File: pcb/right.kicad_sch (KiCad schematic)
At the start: 63 parts, among them J201 Conn_01x06_MountingPin, SW201 SW_SPDT, SW43 SW_Push, SW44 SW_Push, SW45 SW_Push, SW46 SW_Push, SW47 SW_Push, SW48 SW_Push, SW50 SW_Push, SW51 SW_Push, SW52 SW_Push, SW53 SW_Push, SW54 SW_Push, SW55 SW_Push, SW57 SW_Push, SW58 SW_Push, SW59 SW_Push, SW60 SW_Push, SW61 SW_Push, SW62 SW_Push, SW63 SW_Push, SW64 SW_Push, SW65 SW_Push, SW69 SW_Push, SW70 SW_Push, U201 XIAO nRF52840 Plus, U202 XCL103D503CR-G, U203 XC8111AA01MR-G

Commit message: WIP: checkpoint single-XIAO PCB and vertical PHD conversion
Preserve the current single-controller PCB, schematics, documentation, and manufacturing artifacts. Include the vertical PHD placement/routing experiment; its candidate boards still fail DRC and are not production-ready.
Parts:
- removed BT201: GB-BH-4X1-WP, Library:battery_holder_AAA_1x_P55mm, symbol Torabo:Block2
- removed C201: 10uF 25V X5R, Capacitor_SMD:C_0805_2012Metric, symbol Torabo:Block2
- removed C202: 10uF 16V X5R, Capacitor_SMD:C_0603_1608Metric, symbol Torabo:Block2
- removed C203, C204: 0.1uF 50V X7R, Capacitor_SMD:C_0603_1608Metric, symbol Torabo:Block2
- removed R201: 10k, Resistor_SMD:R_0603_1608Metric, symbol Torabo:Block2
- removed R202: 100k, Resistor_SMD:R_0603_1608Metric, symbol Torabo:Block2
- removed SW201: SW_SPDT, Library:ISH-1260-HA-G, symbol Torabo:Block3
- removed TP203: RESET, TestPoint:TestPoint_Pad_D1.5mm, symbol Torabo:Block1
- removed U202: XCL103D503CR-G, Library:CL-2025-02, symbol Torabo:Block9
- removed U203: XC8111AA01MR-G, Package_TO_SOT_SMD:SOT-23-5, symbol Torabo:Block5
- added J202: S12B-PHDSS, Connector_JST:JST_PHD_S12B-PHDSS_2x06_P2.00mm_Horizontal, symbol Torabo:Block12
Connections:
- net COL0: now also J202.2 (P2)
- net COL1: now also J202.3 (P3)
- net COL2: now also J202.4 (P4)
- net COL3: now also J202.5 (P5)
- net COL4: now also J202.6 (P6)
- net COL5: now also J202.7 (P7)
- net COL6: now also J202.8 (P8)
- net GND: now also J202.1 (P1)
- net SYS_3V3: now also J201.6 (P6)
- net LROW3: now reaches U201.19 (P19)
- net LROW3: now also J202.12 (P12)
- net RESET_N: no longer names the net of U201.26 (P26)
- net ROW0 renamed LROW1
- net LROW1: now also J202.10 (P10)
- net ROW1 renamed RROW0
- net ROW2 renamed RROW1
- net ROW3 renamed RROW2
- net ROW4 renamed RROW3
- net SYS_5V: no longer names the net of U201.14 (P14)
- net VBAT_ADC renamed LROW0
- net LROW0: now also J202.9 (P9)
- net VCC renamed LROW2
- net LROW2: now also J202.11 (P11); no longer J201.6 (P6)
- no-connect marks 7 -> 4
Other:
- moved on the sheet: J201, TP201, TP202, TP204, TP205, U201

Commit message: Use vertical JST PHD connectors on split PCBs
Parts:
- J202: value S12B-PHDSS -> B12B-PHDSS; footprint Connector_JST:JST_PHD_S12B-PHDSS_2x06_P2.00mm_Horizontal -> Connector_JST:JST_PHD_B12B-PHDSS_2x06_P2.00mm_Vertical
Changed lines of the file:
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@@
 			(effects (font (size 1.0 1.0)))
 		)
-		(property "Value" "S12B-PHDSS"
+		(property "Value" "B12B-PHDSS"
 			(at 22.860 231.140 0)
 			(effects (font (size 1.0 1.0)))
 		)
-		(property "Footprint" "Connector_JST:JST_PHD_S12B-PHDSS_2x06_P2.00mm_Horizontal"
+		(property "Footprint" "Connector_JST:JST_PHD_B12B-PHDSS_2x06_P2.00mm_Vertical"
 			(at 22.860 210.820 0)
 			(effects (font (size 1.0 1.0)) (hide yes))

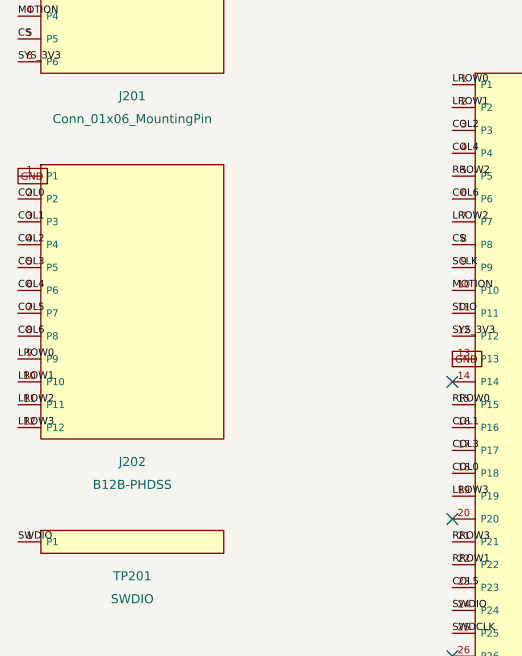
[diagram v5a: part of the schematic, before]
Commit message: Replace split connectors with Samtec FFSD-compatible headers
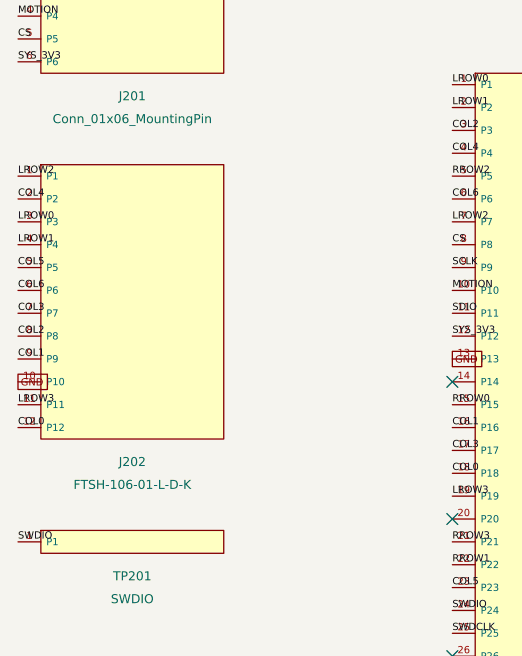
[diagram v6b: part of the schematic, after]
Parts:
- J202: value B12B-PHDSS -> FTSH-106-01-L-D-K; footprint Connector_JST:JST_PHD_B12B-PHDSS_2x06_P2.00mm_Vertical -> Library:Samtec_FTSH-106-01-L-D-K
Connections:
- net COL0: now also J202.12 (P12); no longer J202.2 (P2)
- net COL1: now also J202.9 (P9); no longer J202.3 (P3)
- net COL2: now also J202.8 (P8); no longer J202.4 (P4)
- net COL3: now also J202.7 (P7); no longer J202.5 (P5)
- net COL4: now also J202.2 (P2); no longer J202.6 (P6)
- net COL5: now also J202.5 (P5); no longer J202.7 (P7)
- net COL6: now also J202.6 (P6); no longer J202.8 (P8)
- net GND: now also J202.10 (P10); no longer J202.1 (P1)
- net LROW0: now also J202.3 (P3); no longer J202.9 (P9)
- net LROW1: now also J202.4 (P4); no longer J202.10 (P10)
- net LROW2: now also J202.1 (P1); no longer J202.11 (P11)
- net LROW3: now also J202.11 (P11); no longer J202.12 (P12)
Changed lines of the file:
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@@
 			(effects (font (size 1.0 1.0)))
 		)
-		(property "Value" "B12B-PHDSS"
+		(property "Value" "FTSH-106-01-L-D-K"
 			(at 22.860 231.140 0)
 			(effects (font (size 1.0 1.0)))
 		)
-		(property "Footprint" "Connector_JST:JST_PHD_B12B-PHDSS_2x06_P2.00mm_Vertical"
+		(property "Footprint" "Library:Samtec_FTSH-106-01-L-D-K"
 			(at 22.860 210.820 0)
 			(effects (font (size 1.0 1.0)) (hide yes))
@@
 		)
 	)
+	(label "LROW2"
+		(at 10.160 196.850 0)
+		(effects (font (size 0.8 0.8)) (justify left bottom))
+	)
+	(label "COL4"
+		(at 10.160 199.390 0)
+		(effects (font (size 0.8 0.8)) (justify left bottom))
+	)
+	(label "LROW0"
+		(at 10.160 201.930 0)
+		(effects (font (size 0.8 0.8)) (justify left bottom))
+	)
+	(label "LROW1"
+		(at 10.160 204.470 0)
+		(effects (font (size 0.8 0.8)) (justify left bottom))
+	)
+	(label "COL5"
+		(at 10.160 207.010 0)
+		(effects (font (size 0.8 0.8)) (justify left bottom))
+	)
+	(label "COL6"
+		(at 10.160 209.550 0)
+		(effects (font (size 0.8 0.8)) (justify left bottom))
+	)
+	(label "COL3"
+		(at 10.160 212.090 0)
+		(effects (font (size 0.8 0.8)) (justify left bottom))
+	)
+	(label "COL2"
+		(at 10.160 214.630 0)
+		(effects (font (size 0.8 0.8)) (justify left bottom))
+	)
+	(label "COL1"
+		(at 10.160 217.170 0)
+		(effects (font (size 0.8 0.8)) (justify left bottom))
+	)
 	(global_label "GND"
 		(shape passive)
-		(at 10.160 196.850 0)
+		(at 10.160 219.710 0)
 		(fields_autoplaced yes)
 		(effects (font (size 0.8 0.8)) (justify left bottom))
 	)
-	(label "COL0"
-		(at 10.160 199.390 0)
-		(effects (font (size 0.8 0.8)) (justify left bottom))
-	)
-	(label "COL1"
-		(at 10.160 201.930 0)
-		(effects (font (size 0.8 0.8)) (justify left bottom))
-	)
-	(label "COL2"
-		(at 10.160 204.470 0)
-		(effects (font (size 0.8 0.8)) (justify left bottom))
-	)
-	(label "COL3"
-		(at 10.160 207.010 0)
-		(effects (font (size 0.8 0.8)) (justify left bottom))
-	)
-	(label "COL4"
-		(at 10.160 209.550 0)
-		(effects (font (size 0.8 0.8)) (justify left bottom))
-	)
-	(label "COL5"
-		(at 10.160 212.090 0)
-		(effects (font (size 0.8 0.8)) (justify left bottom))
-	)
-	(label "COL6"
-		(at 10.160 214.630 0)
-		(effects (font (size 0.8 0.8)) (justify left bottom))
-	)
-	(label "LROW0"
-		(at 10.160 217.170 0)
-		(effects (font (size 0.8 0.8)) (justify left bottom))
-	)
-	(label "LROW1"
-		(at 10.160 219.710 0)
-		(effects (font (size 0.8 0.8)) (justify left bottom))
-	)
-	(label "LROW2"
+	(label "LROW3"
 		(at 10.160 222.250 0)
 		(effects (font (size 0.8 0.8)) (justify left bottom))
 	)
-	(label "LROW3"
+	(label "COL0"
 		(at 10.160 224.790 0)
 		(effects (font (size 0.8 0.8)) (justify left bottom))

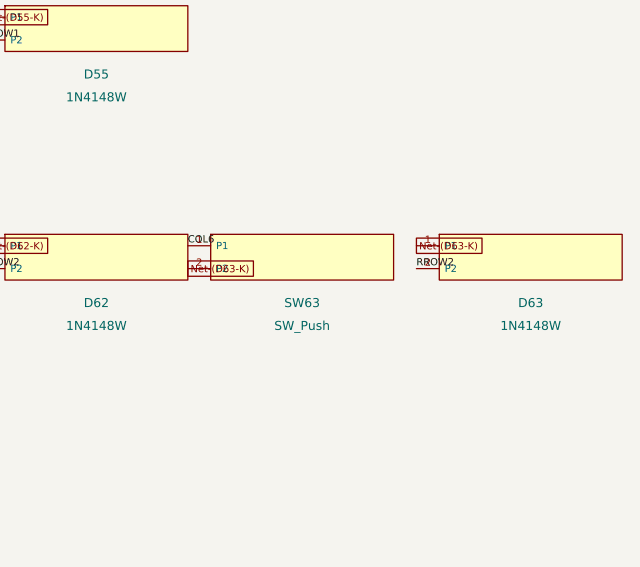
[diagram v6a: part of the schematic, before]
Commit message: Remove key below right split connector
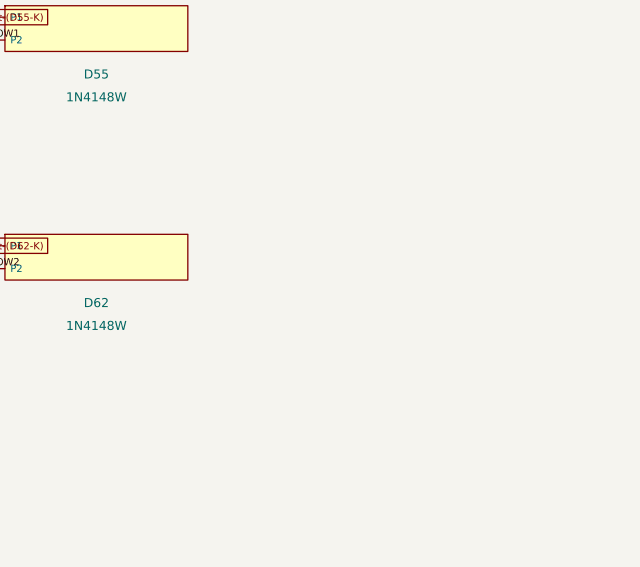
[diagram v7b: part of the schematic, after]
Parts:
- removed D63: 1N4148W, Library:D_SOD-123_HandSoldering, symbol Torabo:Block2
- removed SW63: SW_Push, Library:CHOC_V2_SOCKET_HANDSOLDERING_17mm, symbol Torabo:Block2
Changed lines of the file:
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@@
-	(symbol
-		(lib_id "Torabo:Block2")
-		(at 302.260 78.740 0)
-		(unit 1)
-		(exclude_from_sim no)
-		(in_bom yes)
-		(on_board yes)
-		(dnp no)
-		(property "Reference" "SW63"
-			(at 312.420 83.820 0)
-			(effects (font (size 1.0 1.0)))
-		)
-		(property "Value" "SW_Push"
-			(at 312.420 86.360 0)
-			(effects (font (size 1.0 1.0)))
-		)
-		(property "Footprint" "Library:CHOC_V2_SOCKET_HANDSOLDERING_17mm"
-			(at 312.420 78.740 0)
-			(effects (font (size 1.0 1.0)) (hide yes))
-		)
-		(property "Datasheet" ""
-			(at 312.420 78.740 0)
-			(effects (font (size 1.0 1.0)) (hide yes))
-		)
-		(property "Description" "Generated from PCB connectivity"
-			(at 312.420 78.740 0)
-			(effects (font (size 1.0 1.0)) (hide yes))
-		)
-		(property "LCSC" "C9900009224"
-			(at 312.420 78.740 0)
-			(effects (font (size 1.0 1.0)) (hide yes))
-		)
-		(property "MPN" ""
-			(at 312.420 78.740 0)
-			(effects (font (size 1.0 1.0)) (hide yes))
-		)
-		(pin "1" )
-		(pin "2" )
-		(instances
-			(project "torabo-tsuki-lp-S-ortho-mini"
-				(path "/d470e7a4-966e-4b7e-b716-aac18e0b3811/7368bfa4-9957-402b-978e-3e10016f763f"
-					(reference "SW63")
-					(unit 1)
-				)
-			)
-		)
-	)
-	(label "COL6"
-		(at 299.720 77.470 0)
-		(effects (font (size 0.8 0.8)) (justify left bottom))
-	)
-	(global_label "Net-(D63-K)"
-		(shape passive)
-		(at 299.720 80.010 0)
-		(fields_autoplaced yes)
-		(effects (font (size 0.8 0.8)) (justify left bottom))
-	)
-	(symbol
-		(lib_id "Torabo:Block2")
-		(at 327.660 78.740 0)
-		(unit 1)
-		(exclude_from_sim no)
-		(in_bom yes)
-		(on_board yes)
-		(dnp no)
-		(property "Reference" "D63"
-			(at 337.820 83.820 0)
-			(effects (font (size 1.0 1.0)))
-		)
-		(property "Value" "1N4148W"
-			(at 337.820 86.360 0)
-			(effects (font (size 1.0 1.0)))
-		)
-		(property "Footprint" "Library:D_SOD-123_HandSoldering"
-			(at 337.820 78.740 0)
-			(effects (font (size 1.0 1.0)) (hide yes))
-		)
-		(property "Datasheet" ""
-			(at 337.820 78.740 0)
-			(effects (font (size 1.0 1.0)) (hide yes))
-		)
-		(property "Description" "Generated from PCB connectivity"
-			(at 337.820 78.740 0)
-			(effects (font (size 1.0 1.0)) (hide yes))
-		)
-		(property "LCSC" "C81598"
-			(at 337.820 78.740 0)
-			(effects (font (size 1.0 1.0)) (hide yes))
-		)
-		(property "MPN" "1N4148W"
-			(at 337.820 78.740 0)
-			(effects (font (size 1.0 1.0)) (hide yes))
-		)
-		(pin "1" )
-		(pin "2" )
-		(instances
-			(project "torabo-tsuki-lp-S-ortho-mini"
-				(path "/d470e7a4-966e-4b7e-b716-aac18e0b3811/7368bfa4-9957-402b-978e-3e10016f763f"
-					(reference "D63")
-					(unit 1)
-				)
-			)
-		)
-	)
-	(global_label "Net-(D63-K)"
-		(shape passive)
-		(at 325.120 77.470 0)
-		(fields_autoplaced yes)
-		(effects (font (size 0.8 0.8)) (justify left bottom))
-	)
-	(label "RROW2"
-		(at 325.120 80.010 0)
-		(effects (font (size 0.8 0.8)) (justify left bottom))
-	)
 	(symbol
 		(lib_id "Torabo:Block2")
